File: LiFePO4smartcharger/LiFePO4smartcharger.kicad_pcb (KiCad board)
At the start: 2 copper layers, 99.3 x 98.6 mm, 106 parts, among them J1 Conn_01x02, J10 Conn_01x01, J11 Conn_01x01, J12 Conn_01x04, J14 Conn_01x02, J2 Conn_02x03_Odd_Even, J3 Conn_01x02, J4 Conn_01x02, J5 Conn_01x02, J6 Conn_01x01, J7 Conn_01x01, J8 Conn_01x02, J9 Conn_01x02, Q1 TIP42, Q2 TIP41, Q3 2N3906, Q4 TIP41C, U1 ATMEGA328P-PU, U2 LM358, U3 LCD-016N002L, U4 TL494, U5 LMT85, U9 LM7805_TO220, X3 16MHz

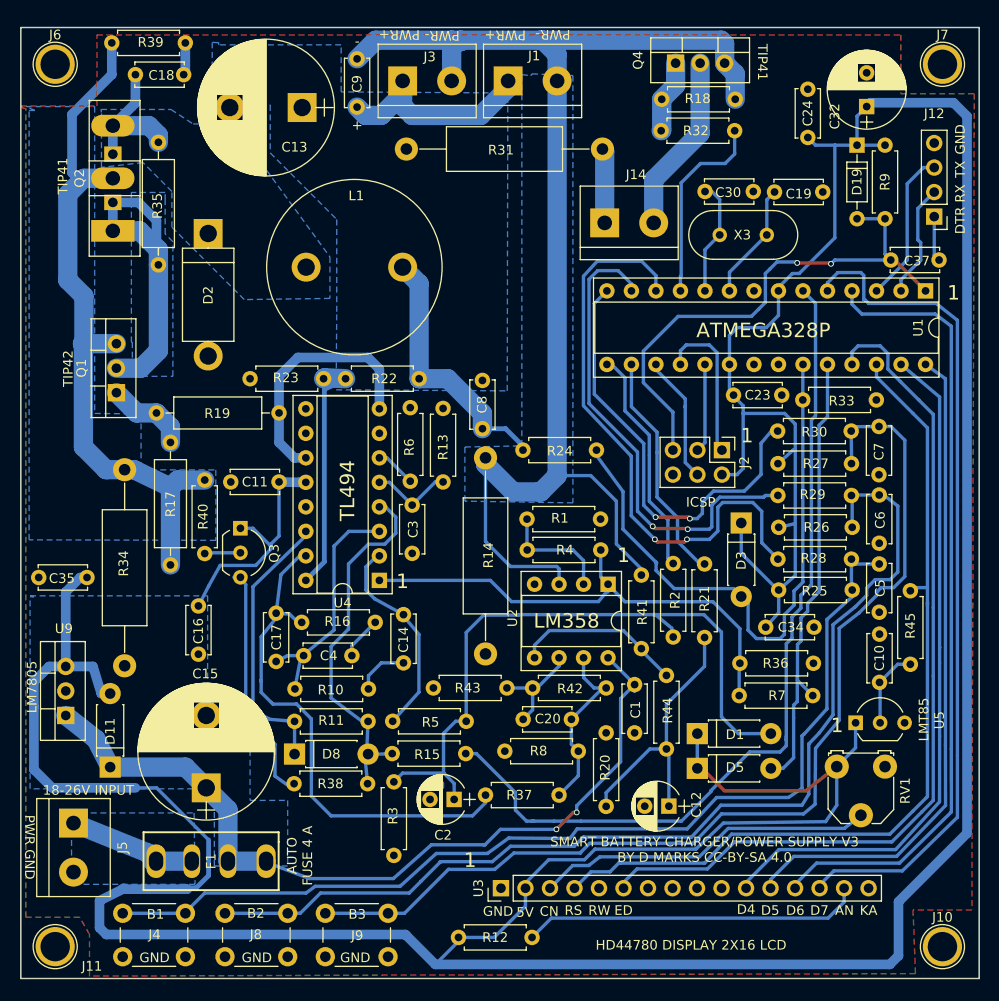
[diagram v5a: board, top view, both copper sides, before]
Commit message: Changed temperature sensor interface
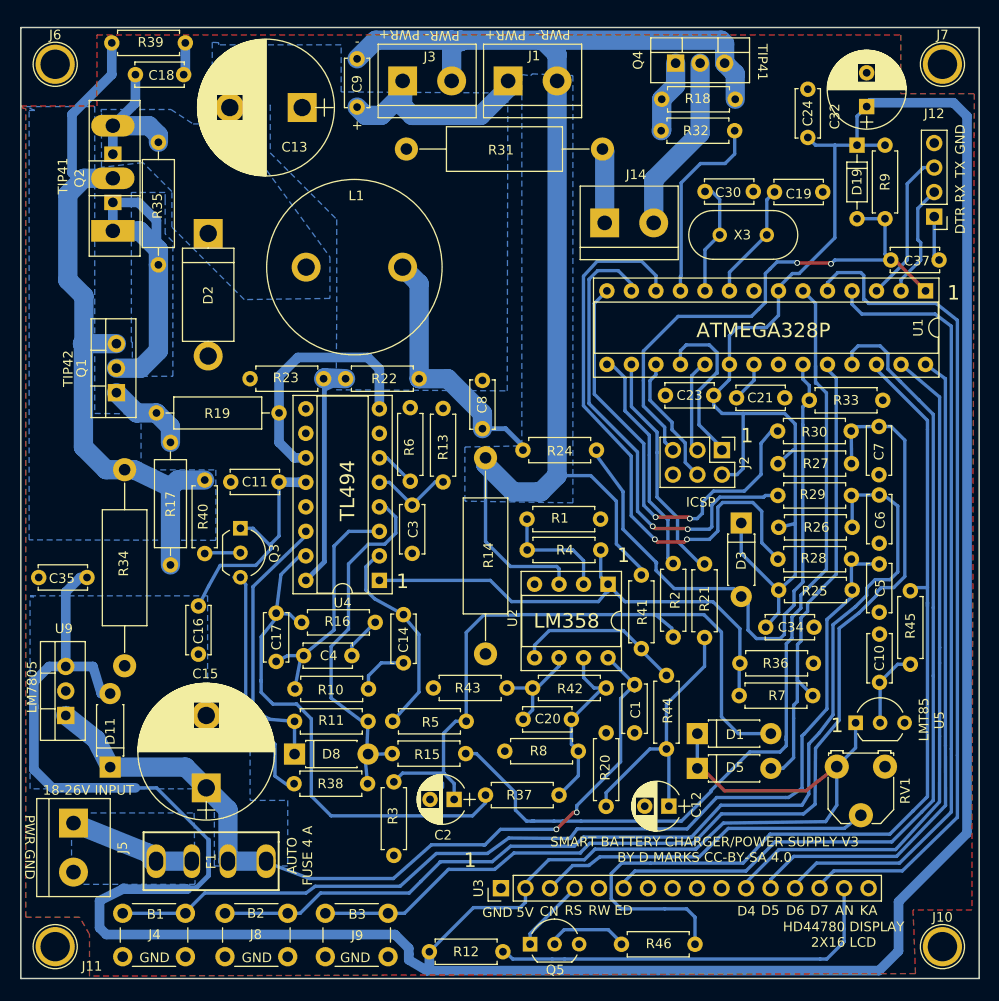
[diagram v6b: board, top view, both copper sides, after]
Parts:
- added C21: 100 nF, Capacitors_THT:C_Disc_D5.0mm_W2.5mm_P5.00mm, F.Cu at (121.4, 68.6)
- added Q5: 2N3906, TO_SOT_Packages_THT:TO-92_Inline_Wide, F.Cu at (95.0, 125.2)
- added R46: 470k, Resistors_THT:R_Axial_DIN0207_L6.3mm_D2.5mm_P7.62mm_Horizontal, F.Cu at (104.5, 125.2)
- moved R12 3.36 mm to (84.6, 126.0)
- moved C23 2.05 mm to (114.0, 68.3), turned to 180 degrees
- moved R33 0.67 mm to (131.6, 68.8)
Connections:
- U3 pad 4: RS -> Net-(Q5-Pad1)
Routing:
- net RS: track 90.0 -> 100.8 mm
- net Net-(Q5-Pad2): track 0.00 -> 10.1 mm
- net Net-(Q5-Pad1): track 0.00 -> 8.40 mm
- net Net-(R12-Pad2): track 35.3 -> 43.0 mm
- net +5V: track 434.8 -> 440.0 mm
- net Net-(C21-Pad2): track 0.00 -> 4.21 mm
- net MISO: track 16.1 -> 18.4 mm
- net SHUTDOWN: track 90.3 -> 92.2 mm
- net MOSI: track 13.7 -> 14.6 mm
- net A1: track 48.6 -> 49.4 mm
- net SCK: track 9.20 -> 9.82 mm
- net A0: track 62.9 -> 63.4 mm

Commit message: Changed to use 5 buttons
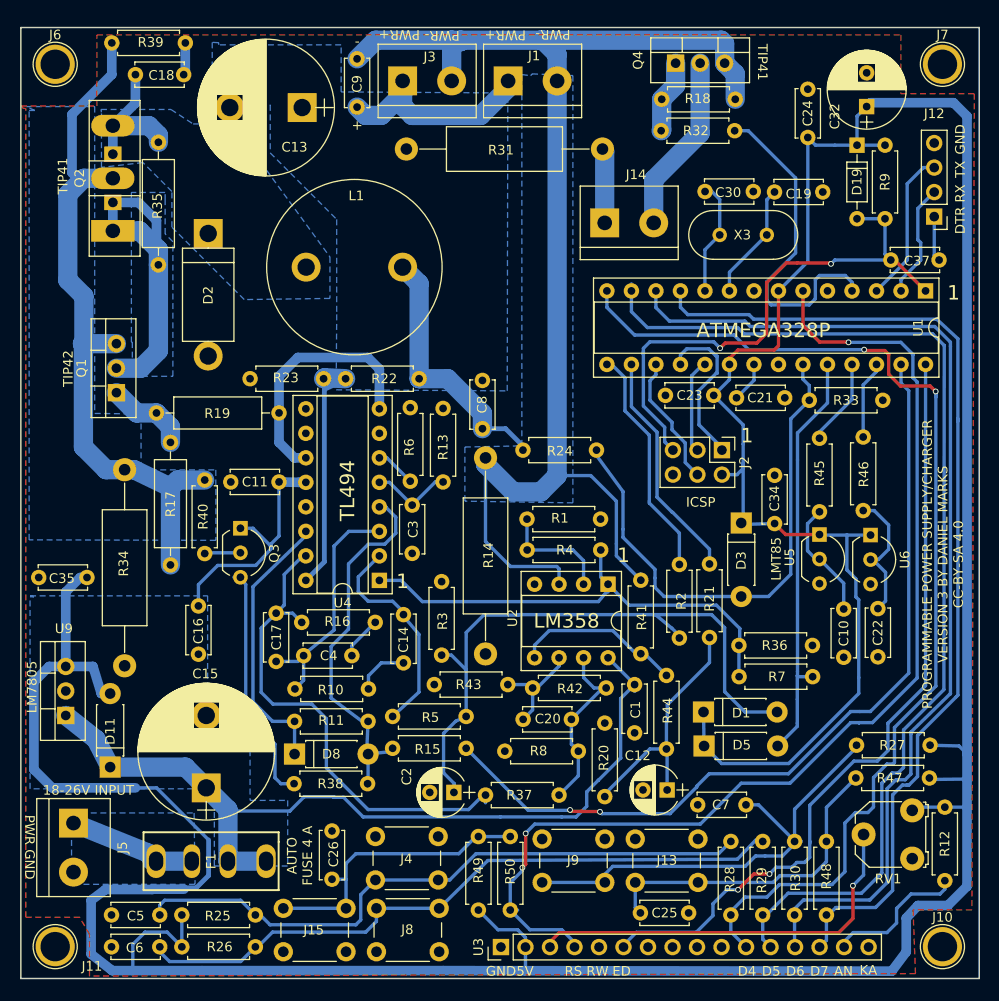
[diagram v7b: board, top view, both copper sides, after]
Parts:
- removed Q5: 2N3906, TO_SOT_Packages_THT:TO-92_Inline_Wide
- added C22: 1000 pF, Capacitors_THT:C_Disc_D5.0mm_W2.5mm_P5.00mm, F.Cu at (131.1, 90.4)
- added C25: 100nF, Capacitors_THT:C_Disc_D5.0mm_W2.5mm_P5.00mm, F.Cu at (106.5, 122.0)
- added C26: 100nF, Capacitors_THT:C_Disc_D5.0mm_W2.5mm_P5.00mm, F.Cu at (74.5, 118.5)
- added J13: Conn_01x02, Buttons_Switches_THT:SW_PUSH_6mm_h4.3mm, F.Cu at (105.9, 114.3)
- added J15: Conn_01x02, Buttons_Switches_THT:SW_PUSH_6mm_h4.3mm, F.Cu at (75.9, 126.0)
- added R47: 1k, Resistors_THT:R_Axial_DIN0207_L6.3mm_D2.5mm_P7.62mm_Horizontal, F.Cu at (128.8, 108.0)
- added R48: 10k, Resistors_THT:R_Axial_DIN0207_L6.3mm_D2.5mm_P7.62mm_Horizontal, F.Cu at (125.7, 122.2)
- added R49: 1k, Resistors_THT:R_Axial_DIN0207_L6.3mm_D2.5mm_P7.62mm_Horizontal, F.Cu at (89.7, 114.0)
- added R50: 10k, Resistors_THT:R_Axial_DIN0207_L6.3mm_D2.5mm_P7.62mm_Horizontal, F.Cu at (93.0, 121.7)
- added U6: LMT85, TO_SOT_Packages_THT:TO-92_Inline_Wide, F.Cu at (130.3, 82.8)
- R25, R26, R27: value 10k -> 1k
- R46: value 470k -> 10k
- moved C6 88.0 mm to (56.6, 125.5), turned to 180 degrees
- moved C5 83.0 mm to (56.6, 122.2), turned to 180 degrees
- moved R26 75.6 mm to (66.5, 125.5)
- moved R25 70.4 mm to (66.5, 122.2)
- moved R46 58.2 mm to (129.5, 72.6), turned to 270 degrees
- moved R12 55.5 mm to (138.0, 111.0), turned to 270 degrees
- moved R30 50.2 mm to (122.4, 122.2), turned to 90 degrees
- moved R29 43.5 mm to (119.1, 122.2), turned to 90 degrees
- moved C7 41.6 mm to (117.4, 110.8), turned to 180 degrees
- moved R28 37.2 mm to (115.8, 122.2), turned to 90 degrees
- moved R27 29.2 mm to (128.8, 104.6), turned to 0 degrees
- moved R3 28.8 mm to (85.9, 87.6), turned to 270 degrees
- moved J4 23.3 mm to (79.0, 114.0), turned to 0 degrees
- moved J9 20.1 mm to (96.3, 114.3), turned to 0 degrees
- moved U5 19.9 mm to (125.0, 82.8), turned to 270 degrees
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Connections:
- R28 pad 1: BUTTON1 -> DB4
- R29 pad 1: BUTTON2 -> DB5
- R30 pad 1: BUTTON3 -> DB6
- R45 pad 1: RS -> TEMP
- R46 pad 1: Net-(Q5-Pad2) -> TEMP2
- R46 pad 2: RS -> Net-(C22-Pad1)
- U1 pad 11: DRAINBASE -> DB7
- U1 pad 12: BUTTON1 -> DB6
- U1 pad 13: BUTTON2 -> DB5
- U1 pad 14: BUTTON3 -> DB4
- U1 pad 25: EDISP -> TEMP
- U1 pad 26: RS -> TEMP2
- U1 pad 27: DB4 -> SHUTDOWN
- U1 pad 28: DB5 -> EDISP
- U1 pad 4: DB6 -> DRAINBASE
- U1 pad 5: DB7 -> Net-(U1-Pad5)
- U1 pad 6: SHUTDOWN -> RS
- U3 pad 4: Net-(Q5-Pad1) -> RS
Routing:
- net BUTTON1: track 61.4 -> 0.00 mm, vias 2 -> 0
- net Net-(C7-Pad1): track 108.9 -> 48.7 mm
- net BUTTON2: track 50.8 -> 0.00 mm, vias 2 -> 0
- net BUTTON3: track 45.7 -> 0.00 mm, vias 2 -> 0
- net DB5: track 69.0 -> 112.8 mm
- net DB4: track 71.4 -> 114.2 mm, vias 0 -> 2
- net Net-(C6-Pad1): track 109.2 -> 69.4 mm
- net Net-(C5-Pad1): track 105.5 -> 66.6 mm
- net Net-(C25-Pad1): track 0.00 -> 34.7 mm
- net Net-(C26-Pad1): track 0.00 -> 30.8 mm
- net Net-(R12-Pad2): track 43.0 -> 15.0 mm
- net DB6: track 82.5 -> 108.3 mm
- net +5V: track 440.0 -> 418.1 mm
- net DB7: track 88.4 -> 104.5 mm
- net DRAINBASE: track 20.5 -> 35.6 mm
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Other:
- board text added: "PROGRAMMABLE POWER SUPPLY/CHARGER VERSION 3 BY DANIEL MARKS CC-BY-SA 4.0"
- board text removed: "B1"
- board text removed: "B2"
- board text removed: "B3"
- board text removed: "CN"
- board text removed: "HD44780 DISPLAY 2X16 LCD"
- board text removed: "SMART BATTERY CHARGER/POWER SUPPLY V3 BY D MARKS CC-BY-SA 4.0"
